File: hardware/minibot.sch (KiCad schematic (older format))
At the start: 12 parts

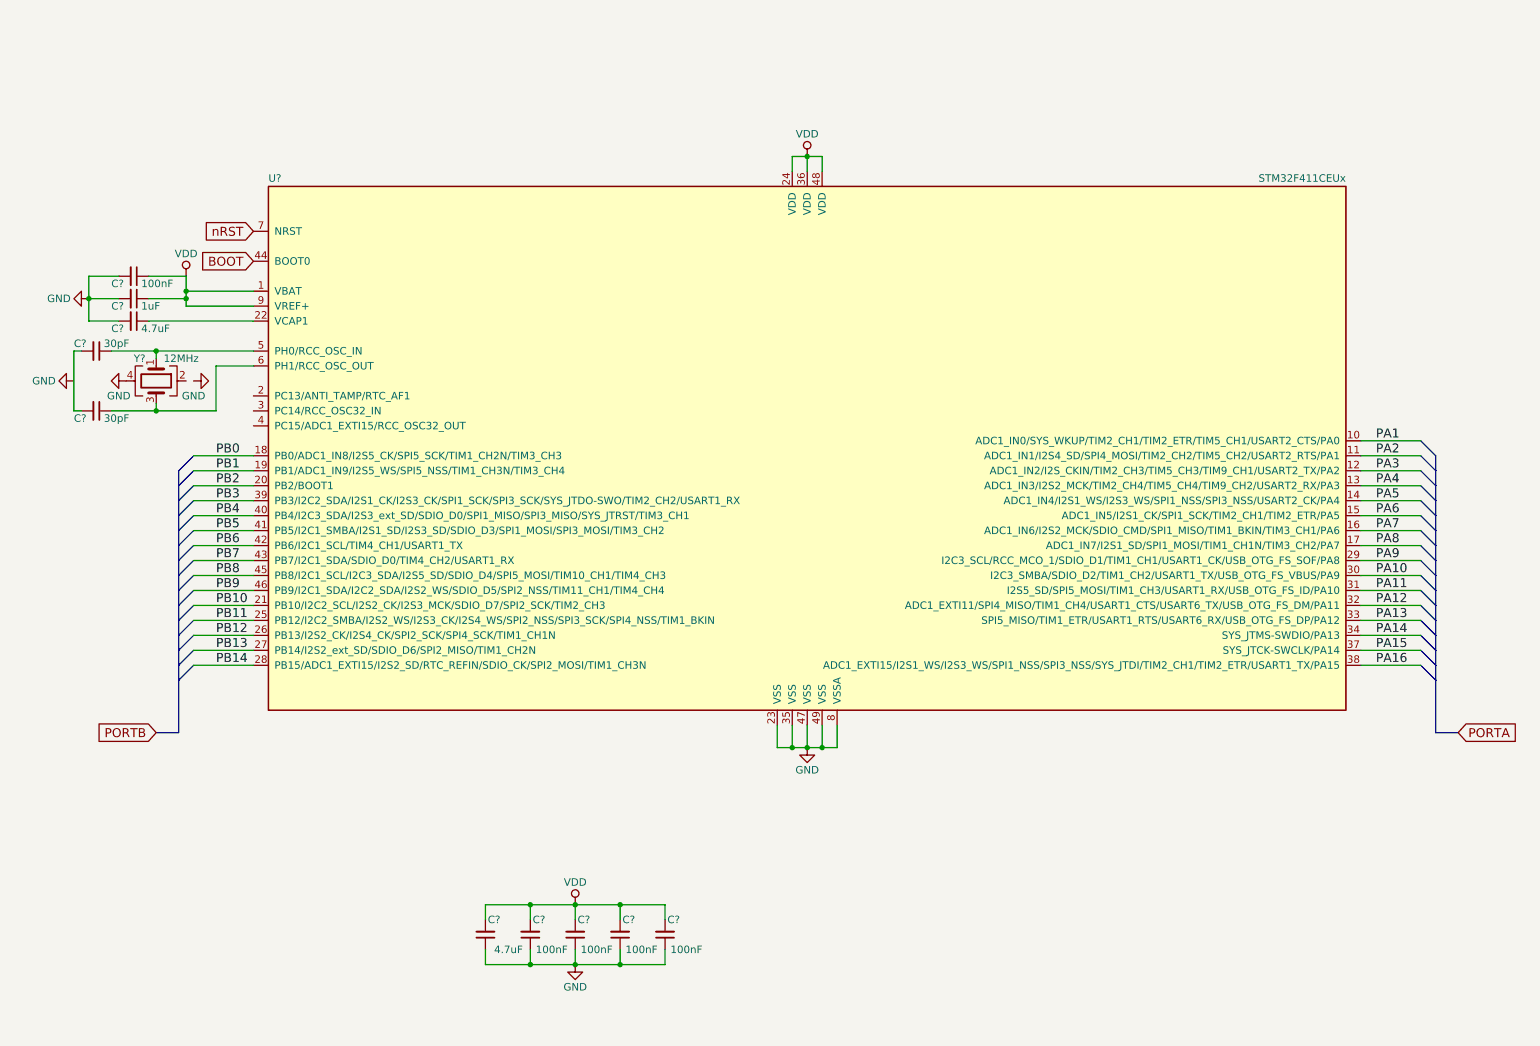
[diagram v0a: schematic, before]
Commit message: Moved the microcontroller to another sheet and setup the boot and reset switches
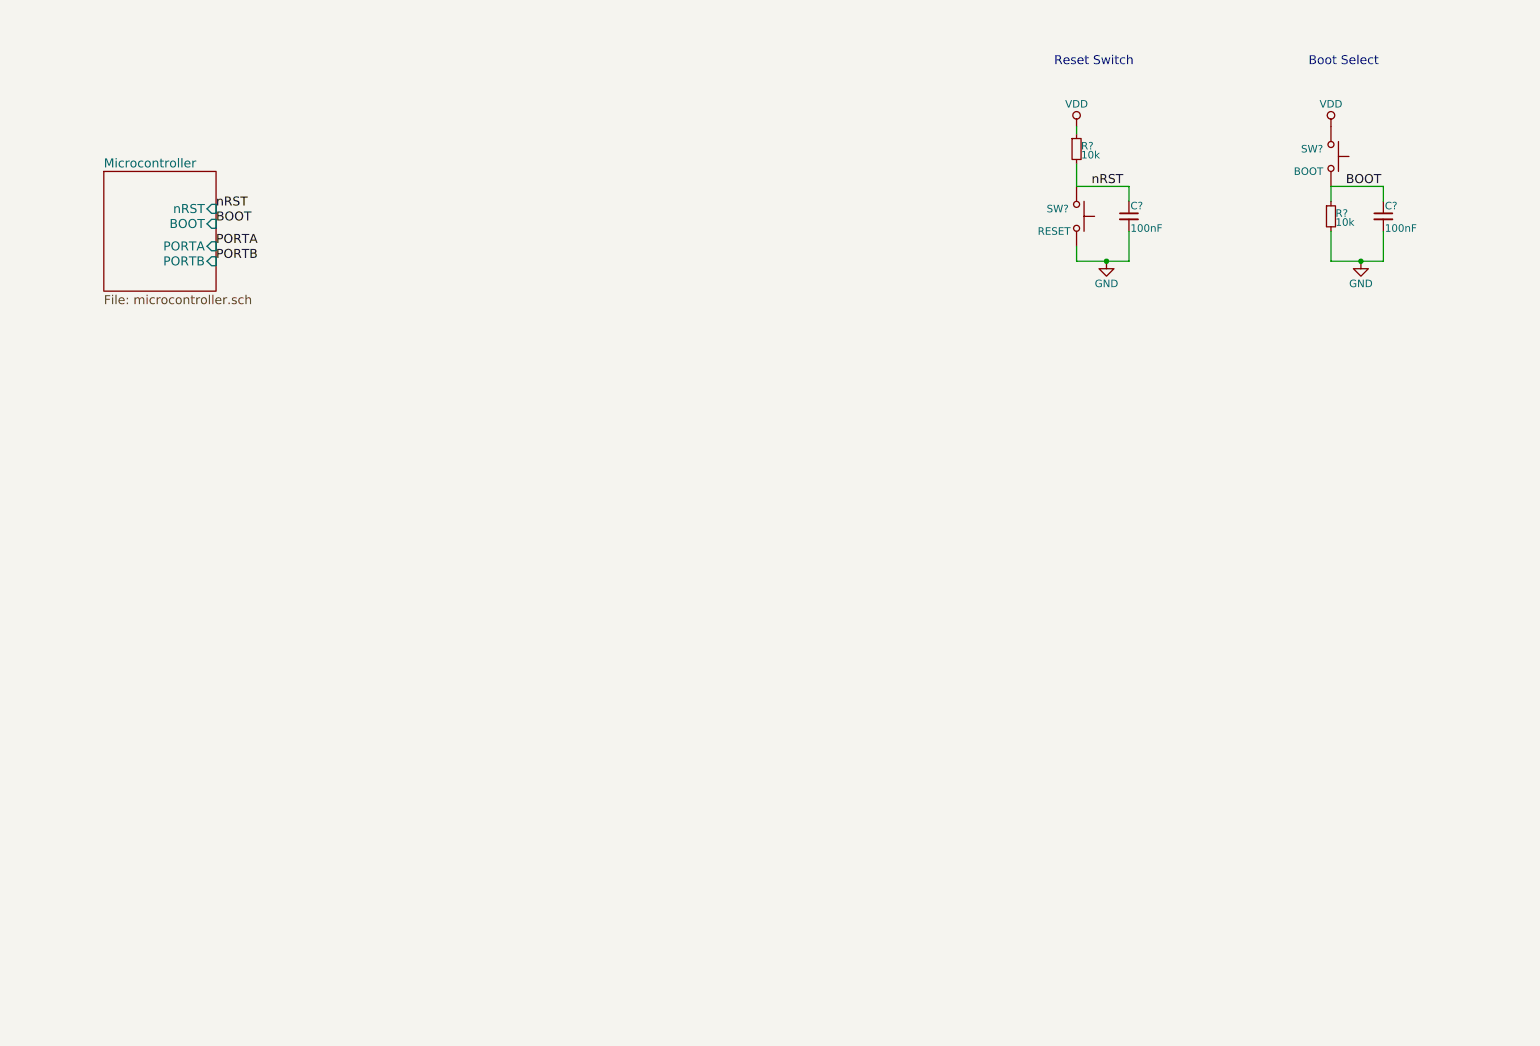
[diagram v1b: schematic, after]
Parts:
- removed C? (x2): 4.7uF, symbol C_Small
- removed C?: 1uF, symbol C_Small
- removed C? (x5): 100nF, symbol C_Small
- removed C? (x2): 30pF, symbol C_Small
- removed U?: STM32F411CEUx, UFQFPN48, symbol STM32F411CEUx
- removed Y?: 12MHz, symbol Crystal_GND24
- added C? (x2): 100nF, symbol C_Small
- added R? (x2): 10k, symbol R_Small
- added SW?: RESET, symbol SW_Push
- added SW?: BOOT, symbol SW_Push
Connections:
- net labels removed: PA1, PA10, PA11, PA12, PA13, PA14, PA15, PA16, PA2, PA3, PA4, PA5, PA6, PA7, PA8, PA9, PB0, PB1, PB10, PB11, PB12, PB13, PB14, PB2, PB3, PB4, PB5, PB6, PB7, PB8, PB9
- wire segments 87 -> 16
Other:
- note added: "Boot Select\n"
- note added: "Reset Switch\n"

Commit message: Add the RN41 radio and a header for the servos
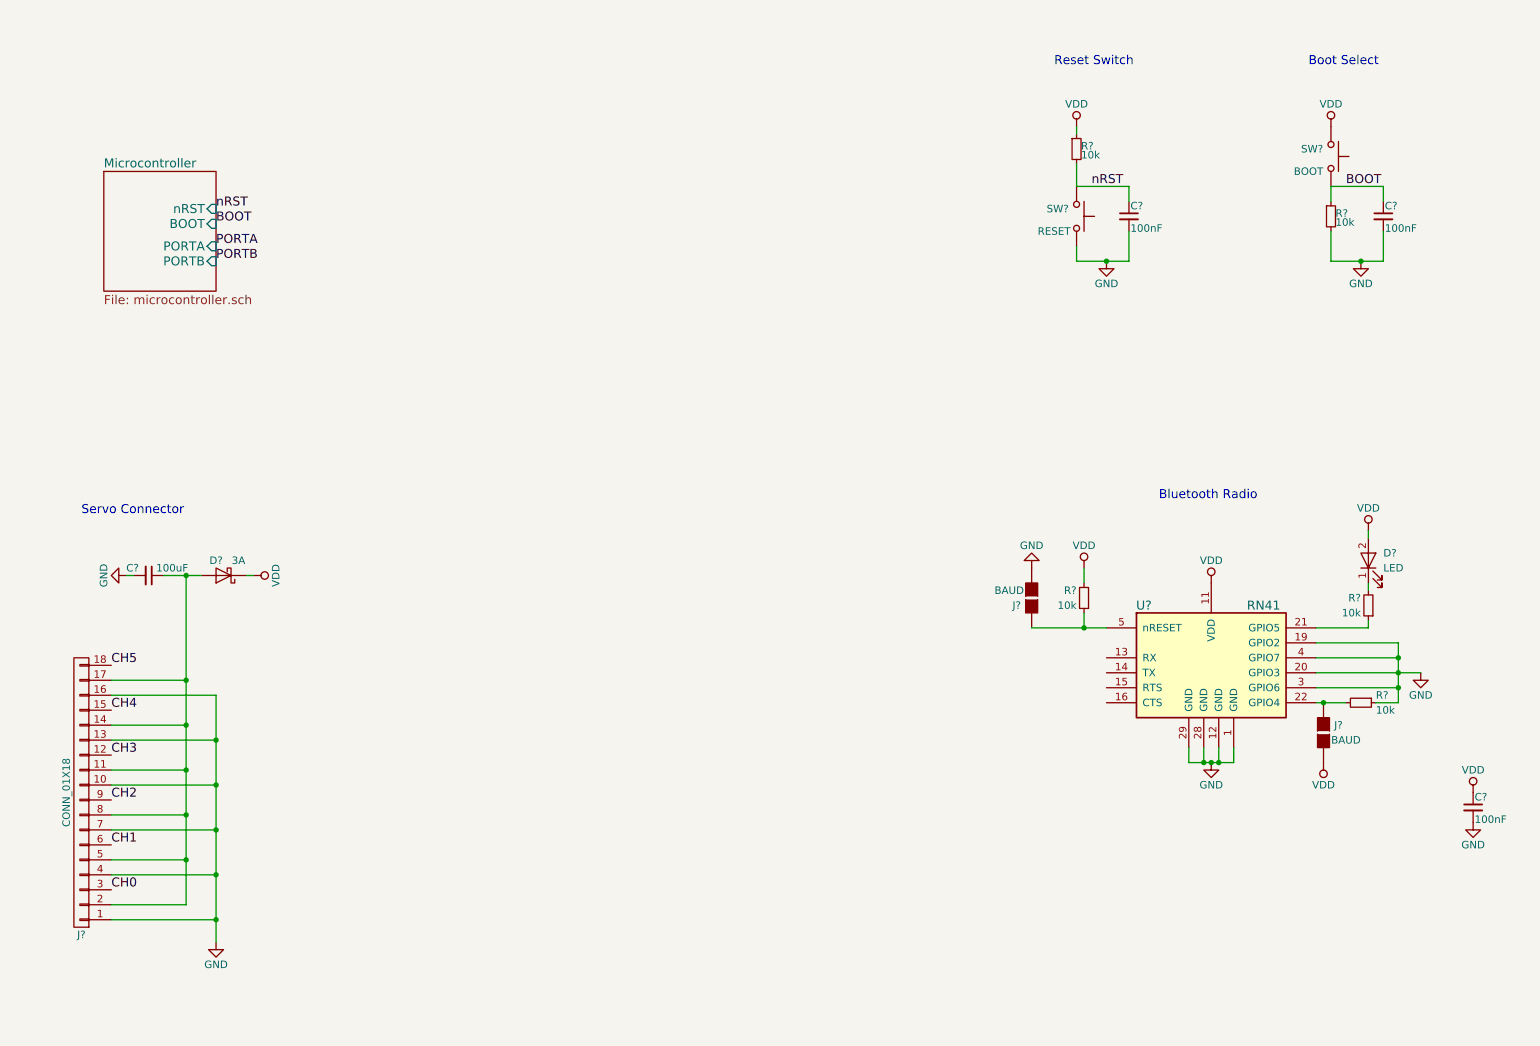
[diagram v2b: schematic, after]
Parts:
- added C?: 100nF, symbol C_Small
- added C?: 100uF, symbol C_Small
- added D?: LED, symbol LED
- added D?: 3A, symbol D_Schottky
- added J? (x2): BAUD, Connectors:GS2, symbol GS2
- added J?: CONN_01X18, symbol CONN_01X18
- added R? (x3): 10k, symbol R_Small
- added U?: RN41, symbol RN41
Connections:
- net GND: now also C?.2, C?.2, J?.1 (P1), J?.10 (P10), J?.13 (P13), J?.16 (P16), J?.2 (G2), J?.4 (P4), J?.7 (P7), R?.1, U?.1 (GND), U?.12 (GND), U?.19 (GPIO2), U?.20 (GPIO3), U?.28 (GND), U?.29 (GND), U?.3 (GPIO6), U?.4 (GPIO7)
- net VDD: now also C?.1, D?.1 (K), D?.2 (A), J?.2 (G2), R?.2, U?.11 (VDD)
- new net: R?.1, U?.21 (GPIO5)
- new net: J?.1 (G1), R?.2, U?.22 (GPIO4)
- new net: J?.1 (G1), R?.1, U?.5 (nRESET)
- new net: D?.1 (K), R?.2
- new net: C?.1, D?.2 (A), J?.11 (P11), J?.14 (P14), J?.17 (P17), J?.2 (P2), J?.5 (P5), J?.8 (P8)
- new net CH0: J?.3 (P3)
- new net CH1: J?.6 (P6)
- new net CH2: J?.9 (P9)
- new net CH3: J?.12 (P12)
- new net CH4: J?.15 (P15)
- new net CH5: J?.18 (P18)
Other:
- note added: "Bluetooth Radio\n"
- note added: "Servo Connector"

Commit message: Add a USB connector and 3.3V regulation
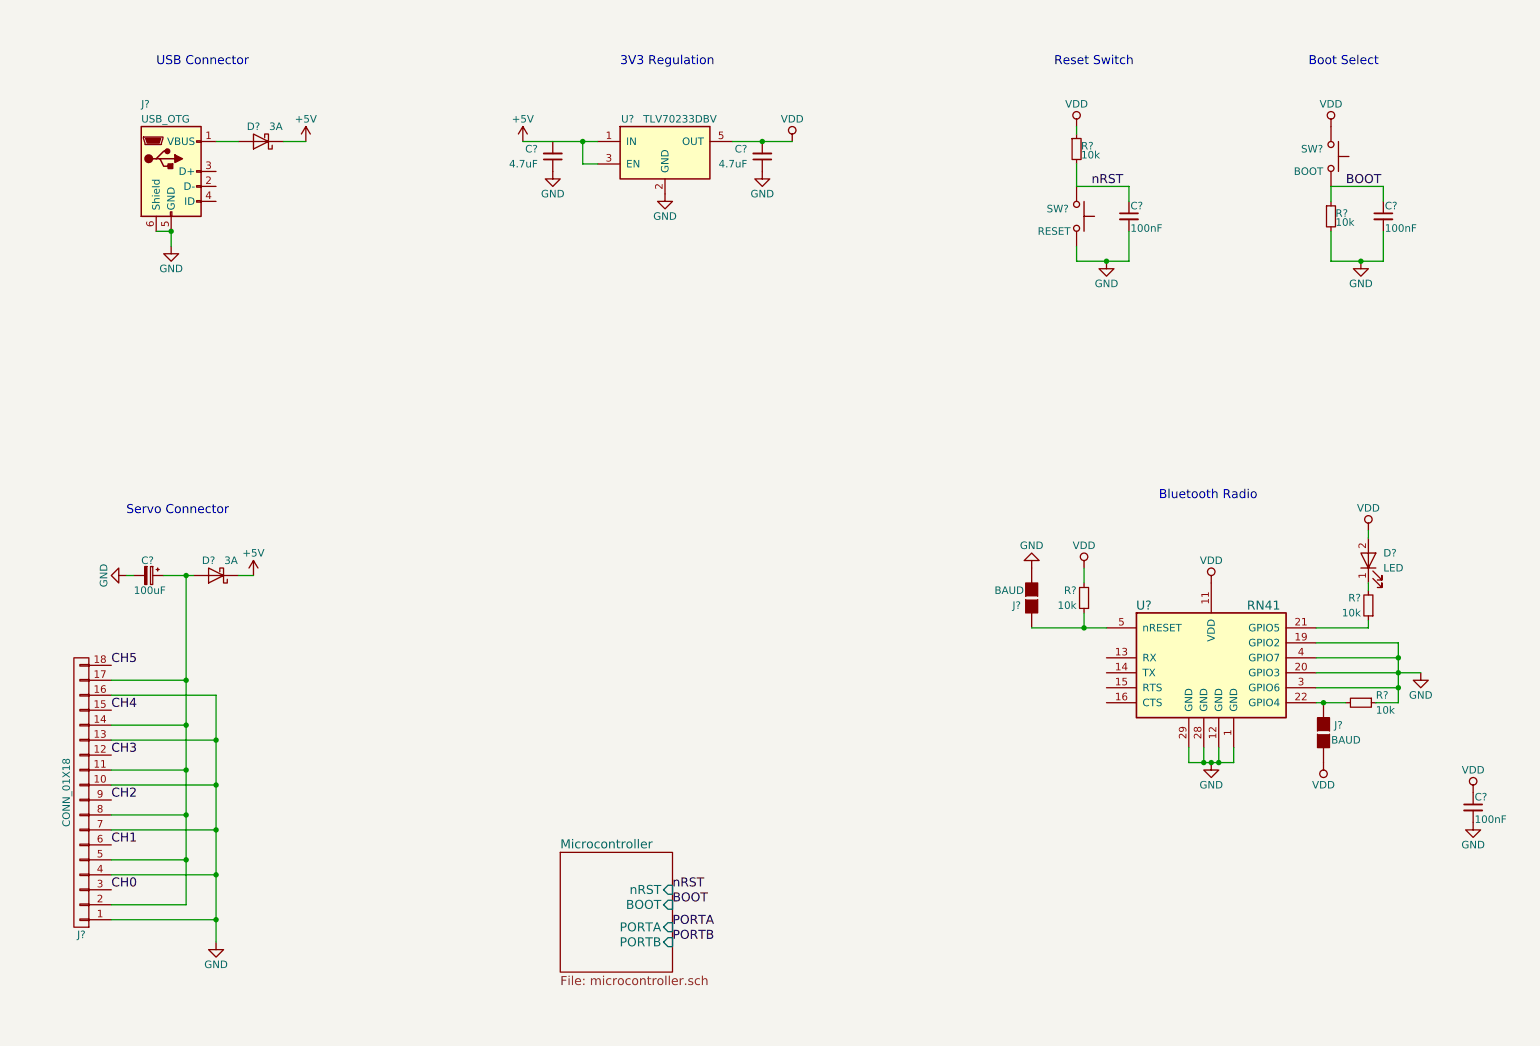
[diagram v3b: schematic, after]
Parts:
- removed C?: 100uF, symbol C_Small
- added C? (x2): 4.7uF, symbol C_Small
- added C?: 100uF, symbol CP_Small
- added D?: 3A, symbol D_Schottky
- added J?: USB_OTG, symbol USB_OTG
- added U?: TLV70233DBV, TO_SOT_Packages_SMD:SOT-23-5, symbol TLV70233DBV
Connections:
- net GND: now also C?.1, C?.1, C?.2, J?.5 (GND), J?.6 (Shield), U?.2 (GND)
- net VDD: now also C?.2, U?.5 (OUT); no longer D?.1 (K)
- net at J?.11 (P11), J?.14 (P14), J?.17 (P17)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: now also C?.1, D?.2 (A); no longer D?.2 (A)
- new net: D?.2 (A), J?.1 (VBUS)
- new net +5V: D?.1 (K), D?.1 (K), U?.1 (IN), U?.3 (EN)
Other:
- note added: "3V3 Regulation\n"
- note added: "USB Connector\n"
- moved on the sheet: D?

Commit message: Broke out the A and B PIO ports. Added status LEDs
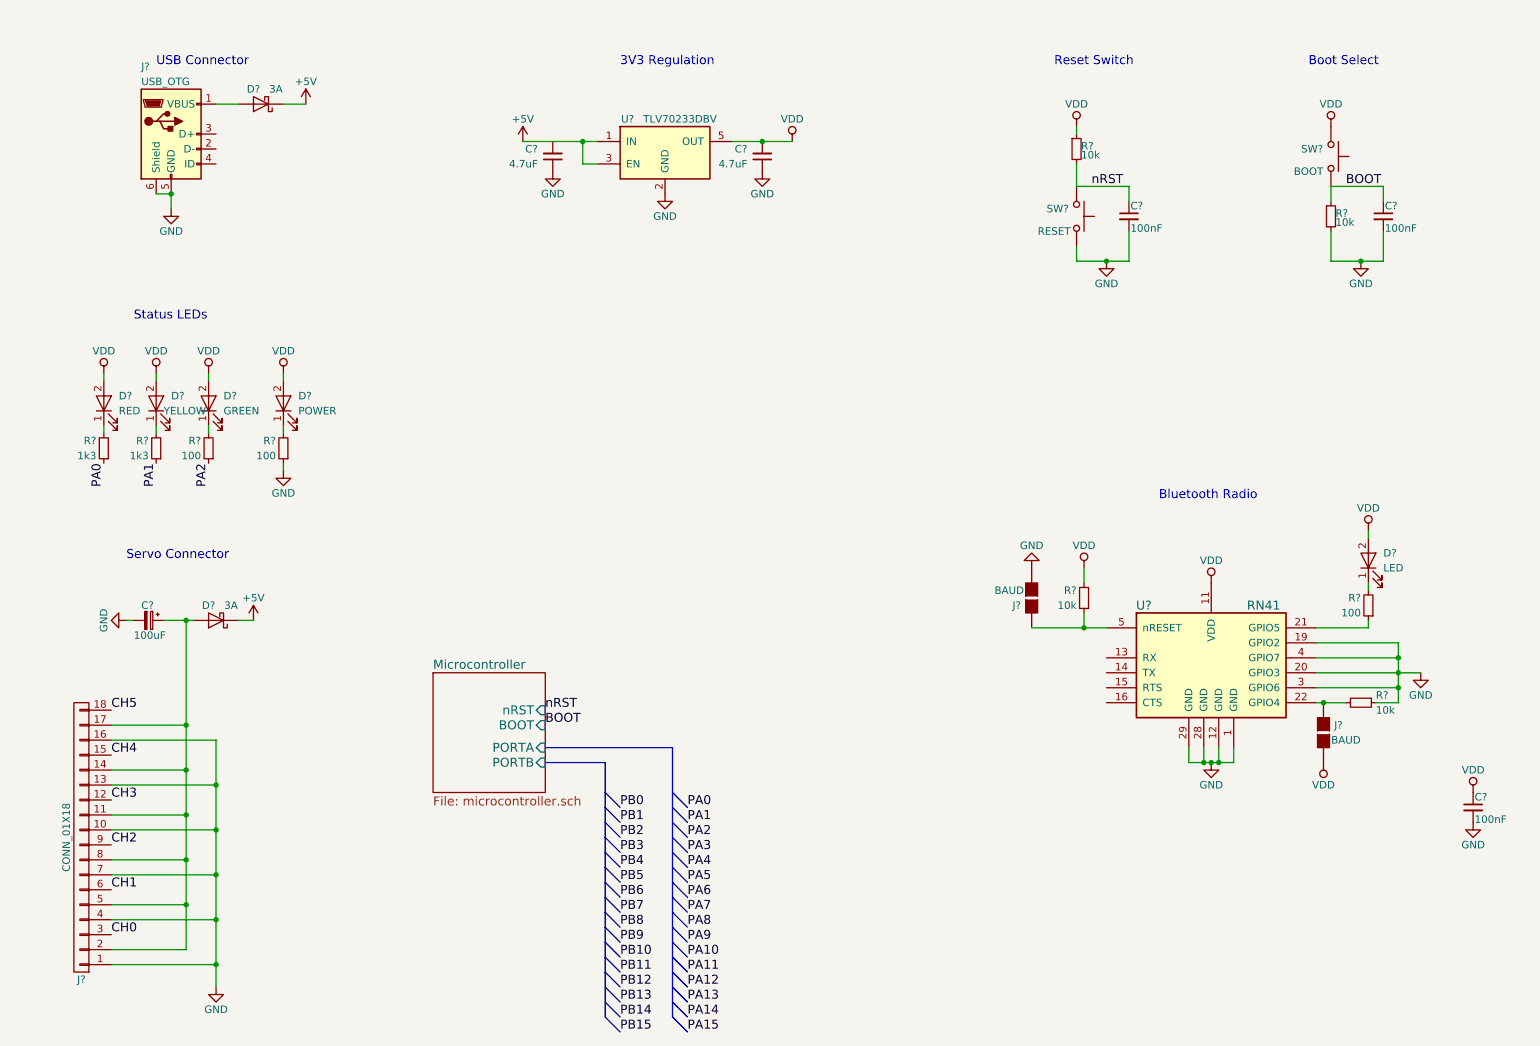
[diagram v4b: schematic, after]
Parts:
- added D?: RED, symbol LED
- added D?: YELLOW, symbol LED
- added D?: GREEN, symbol LED
- added D?: POWER, symbol LED
- added R? (x2): 1k3, symbol R_Small
- added R? (x2): 100, symbol R_Small
- R?: value 10k -> 100
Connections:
- net GND: now also R?.1
- net VDD: now also D?.2 (A), D?.2 (A), D?.2 (A), D?.2 (A)
- new net: D?.1 (K), R?.2 (x4)
- new net PA0: R?.1
- new net PA1: R?.1
- new net PA2: R?.1
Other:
- note added: "Status LEDs\n"
- moved on the sheet: C?, D?, J?
